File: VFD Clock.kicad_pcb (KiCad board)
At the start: 2 copper layers, 28 parts, among them U1 74HC595, U10 74HC595, U11 UDN2981A, U12 IV-11 VFD Tube, U13 74HC595, U14 UDN2981A, U15 IV-11 VFD Tube, U16 74HC595, U17 UDN2981A, U18 IV-11 VFD Tube, U19 XL6009 Module, U2 UDN2981A, U20 LM2596 Module, U3 IV-11 VFD Tube, U4 74HC595, U5 UDN2981A, U6 IV-11 VFD Tube, U7 74HC595, U8 UDN2981A, U9 IV-11 VFD Tube

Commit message: pcb layout updates. Locked in the tube positions
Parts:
- U12: value IV-11 VFD Tube -> Minute Right
- U15: value IV-11 VFD Tube -> Second Left
- U18: value IV-11 VFD Tube -> Second Right
- U3: value IV-11 VFD Tube -> Hour Left
- U6: value IV-11 VFD Tube -> Hour Right
- U9: value IV-11 VFD Tube -> Minute Left
- moved U20 121.2 mm to (138.1, 153.7), turned to 180 degrees
- moved U17 74.4 mm to (243.8, 81.8)
- moved U16 72.0 mm to (261.2, 119.0)
- moved U18 71.8 mm to (251.0, 100.0)
- moved U19 70.5 mm to (189.4, 152.4), turned to 180 degrees
- moved A1 52.9 mm to (214.5, 151.0), turned to 90 degrees
- moved U1 40.8 mm to (108.1, 116.4)
- moved U7 40.8 mm to (172.1, 119.4)
- moved U9 40.5 mm to (162.0, 100.0)
- moved U3 40.1 mm to (100.0, 100.0)
- moved U2 40.0 mm to (89.8, 82.6)
- moved U12 38.6 mm to (189.0, 100.0)
- moved U4 38.3 mm to (135.9, 117.2)
- moved U10 38.2 mm to (197.8, 119.4)
- moved U8 37.5 mm to (150.8, 83.0)
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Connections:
- net /D2 renamed /Mode_Button
- net /D3 renamed /Up_Button
- net /D4 renamed /Down_Button
- net /D5 renamed /Select_Button

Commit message: PCB layout changes
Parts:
- moved C10 317.5 mm to (88.0, 120.0), turned to 90 degrees
- moved C9 288.6 mm to (118.0, 120.0), turned to 90 degrees
- moved C8 259.9 mm to (148.0, 120.0), turned to 90 degrees
- moved C7 231.6 mm to (178.0, 120.0), turned to 90 degrees
- moved C1 199.6 mm to (221.0, 130.0), turned to 180 degrees
- moved C11 199.4 mm to (208.0, 120.0), turned to 90 degrees
- moved C12 168.7 mm to (239.0, 120.0), turned to 90 degrees
- moved U13 6.75 mm to (229.0, 115.0)
- moved U7 5.35 mm to (169.0, 115.0)
- moved U10 4.55 mm to (199.0, 115.0)
- moved U16 4.19 mm to (260.0, 115.0)
- moved U4 3.76 mm to (139.1, 115.2)
- moved U5 3.12 mm to (121.1, 84.0)
- moved U11 2.95 mm to (181.5, 84.0)
- moved U17 2.86 mm to (242.0, 84.0)
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
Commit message: pcb layout
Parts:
- moved U20 54.4 mm to (91.1, 126.3), turned to 0 degrees
- moved U19 42.8 mm to (154.6, 127.6), turned to 0 degrees
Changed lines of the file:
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@@
 		)
 		(property "Value" "UDN2981A"
-			(at -11 -3.74 0)
+			(at -10 -4.16 0)
 			(layer "F.Fab")
 			(effects
@@
 		)
 		(property "Value" "UDN2981A"
-			(at 10.46468 4.04836 90)
+			(at -10 -5 180)
 			(layer "F.Fab")
 			(effects
@@
 	(footprint "Custom Parts:LM2596 Module"
 		(layer "F.Cu")
-		(at 138.14 153.66 180)
+		(at 91.14 126.34)
 		(property "Reference" "U20"
-			(at 25.4 8.66 180)
+			(at 25.4 8.66 0)
 			(unlocked yes)
 			(layer "F.SilkS")
@@
 		)
 		(property "Value" "LM2596 Module"
-			(at 25.4 10.16 180)
+			(at 25.4 10.16 0)
 			(unlocked yes)
 			(layer "F.Fab")
@@
 		)
 		(property "Datasheet" ""
-			(at 0 0 180)
+			(at 0 0 0)
 			(unlocked yes)
 			(layer "F.Fab")
@@
 		)
 		(property "Description" "LM2596 Module from Aliexpress"
-			(at 0 0 180)
+			(at 0 0 0)
 			(unlocked yes)
 			(layer "F.Fab")
@@
 		(duplicate_pad_numbers_are_jumpers no)
 		(fp_line
-			(start 48 23)
+			(start 0 0)
 			(end 0 23)
 			(stroke
@@
 		)
 		(fp_line
-			(start 48 0)
-			(end 48 23)
+			(start 0 0)
+			(end 48 0)
 			(stroke
 				(width 0.1)
@@
 		)
 		(fp_line
-			(start 0 0)
-			(end 48 0)
+			(start 48 0)
+			(end 48 23)
 			(stroke
 				(width 0.1)
@@
 		)
 		(fp_line
-			(start 0 0)
+			(start 48 23)
 			(end 0 23)
 			(stroke
@@
 		)
 		(fp_text user "${REFERENCE}"
-			(at 25.4 11.66 180)
+			(at 25.4 11.66 0)
 			(unlocked yes)
 			(layer "F.Fab")
@@
 		)
 		(pad "1" thru_hole circle
-			(at 1.14 1.34 180)
+			(at 1.14 1.34)
 			(size 1.8 1.8)
 			(drill 1)
@@
 		)
 		(pad "2" thru_hole circle
-			(at 1.14 21.66 180)
+			(at 1.14 21.66)
 			(size 1.8 1.8)
 			(drill 1)
@@
 		)
 		(pad "3" thru_hole circle
-			(at 46.86 1.34 180)
+			(at 46.86 1.34)
 			(size 1.8 1.8)
 			(drill 1)
@@
 		)
 		(pad "4" thru_hole circle
-			(at 46.86 21.66 180)
+			(at 46.86 21.66)
 			(size 1.8 1.8)
 			(drill 1)
@@
 		)
 		(property "Value" "UDN2981A"
-			(at 10.46468 4.04836 90)
+			(at -10 -4.696 180)
 			(layer "F.Fab")
 			(effects
@@
 		)
 		(property "Value" "UDN2981A"
-			(at 10.46468 4.04836 90)
+			(at -10 -3.928 180)
 			(layer "F.Fab")
 			(effects
@@
 		)
 		(property "Value" "UDN2981A"
-			(at 10.46468 4.04836 90)
+			(at -10 -5.464 180)
 			(layer "F.Fab")
 			(effects
@@
 	(footprint "Custom Parts:XL6009 Module"
 		(layer "F.Cu")
-		(at 189.4394 152.4285 180)
+		(at 154.5606 127.5715)
 		(property "Reference" "U19"
-			(at 21 11 180)
+			(at 21 11 0)
 			(unlocked yes)
 			(layer "F.SilkS")
@@
 		)
 		(property "Value" "XL6009 Module"
-			(at 21 7.5 180)
+			(at 21 7.5 0)
 			(unlocked yes)
 			(layer "F.Fab")
@@
 		)
 		(property "Datasheet" ""
-			(at 0 0 180)
+			(at 0 0 0)
 			(unlocked yes)
 			(layer "F.Fab")
@@
 		)
 		(property "Description" "XL6009 Module from Aliexpress"
-			(at 0 0 180)
+			(at 0 0 0)
 			(unlocked yes)
 			(layer "F.Fab")
@@
 		(duplicate_pad_numbers_are_jumpers no)
 		(fp_line
-			(start 43 21)
-			(end 0 21)
+			(start 0 0)
+			(end 43 0)
 			(stroke
 				(width 0.1)
@@
 		)
 		(fp_line
-			(start 43 0)
-			(end 43 21)
+			(start 0 21)
+			(end 0 0)
 			(stroke
 				(width 0.1)
@@
 		)
 		(fp_line
-			(start 0 21)
-			(end 0 0)
+			(start 43 0)
+			(end 43 21)
 			(stroke
 				(width 0.1)
@@
 		)
 		(fp_line
-			(start 0 0)
-			(end 43 0)
+			(start 43 21)
+			(end 0 21)
 			(stroke
 				(width 0.1)
@@
 		)
 		(fp_line
-			(start 43.1038 21.082)
-			(end -0.0762 21.082)
+			(start -0.0762 21.082)
+			(end -0.0762 -0.1016)
 			(stroke
 				(width 0.05)
@@
 		)
 		(fp_line
-			(start 43.1038 -0.1016)
-			(end 43.1038 21.082)
+			(start -0.0508 -0.1016)
+			(end -0.0762 -0.1016)
 			(stroke
 				(width 0.05)
@@
 		)
 		(fp_line
-			(start -0.0508 -0.1016)
-			(end -0.0762 -0.1016)
+			(start 43.1038 -0.1016)
+			(end 43.1038 21.082)
 			(stroke
 				(width 0.05)
@@
 		)
 		(fp_line
-			(start -0.0762 21.082)
-			(end -0.0762 -0.1016)
+			(start 43.1038 21.082)
+			(end -0.0762 21.082)
 			(stroke
 				(width 0.05)
@@
 			(layer "F.CrtYd")
 		)
-		(fp_text user "Out-"
-			(at 36.9316 19.9898 180)
+		(fp_text user "In-"
+			(at 2.4638 19.8882 0)
 			(unlocked yes)
 			(layer "F.SilkS")
@@
 			)
 		)
-		(fp_text user "Out+"
-			(at 36.8808 2.1844 180)
+		(fp_text user "In+"
+			(at 2.6162 2.2352 0)
 			(unlocked yes)
 			(layer "F.SilkS")
@@
 			)
 		)
-		(fp_text user "In+"
-			(at 2.6162 2.2352 180)
+		(fp_text user "Out+"
+			(at 36.8808 2.1844 0)
 			(unlocked yes)
 			(layer "F.SilkS")
@@
 			)
 		)
-		(fp_text user "In-"
-			(at 2.4638 19.8882 180)
+		(fp_text user "Out-"
+			(at 36.9316 19.9898 0)
 			(unlocked yes)
 			(layer "F.SilkS")
@@
 		)
 		(fp_text user "${REFERENCE}"
-			(at 21 9 180)
+			(at 21 9 0)
 			(unlocked yes)
 			(layer "F.Fab")
@@
 		)
 		(pad "1" thru_hole circle
-			(at 1.18 1.61 180)
+			(at 1.18 1.61)
 			(size 1.8 1.8)
 			(drill 1)
@@
 		)
 		(pad "2" thru_hole circle
-			(at 1.18 19.39 180)
+			(at 1.18 19.39)
 			(size 1.8 1.8)
 			(drill 1)
@@
 		)
 		(pad "3" thru_hole circle
-			(at 41.82 1.61 180)
+			(at 41.82 1.61)
 			(size 1.8 1.8)
 			(drill 1)
@@
 		)
 		(pad "4" thru_hole circle
-			(at 41.82 19.39 180)
+			(at 41.82 19.39)
 			(size 1.8 1.8)
 			(drill 1)
@@
 		)
 		(property "Value" "UDN2981A"
-			(at 10.46468 4.04836 90)
+			(at -10 -5.232 180)
 			(layer "F.Fab")
 			(effects

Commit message: minor changes
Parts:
- added J2: Mode Button, Connector_JST:JST_XH_B2B-XH-A_1x02_P2.50mm_Vertical, F.Cu at (187.5, 143.5)
- added J3: Up Button, Connector_JST:JST_XH_B2B-XH-A_1x02_P2.50mm_Vertical, F.Cu at (197.5, 143.5)
- added J4: Down Button, Connector_JST:JST_XH_B2B-XH-A_1x02_P2.50mm_Vertical, F.Cu at (207.0, 143.5)
- added J5: Select Button, Connector_JST:JST_XH_B2B-XH-A_1x02_P2.50mm_Vertical, F.Cu at (217.0, 143.5)
- moved A1 152.9 mm to (68.0, 107.0), turned to 0 degrees
- moved C1 142.0 mm to (82.5, 98.5)
- moved U19 17.5 mm to (137.1, 126.6)
- moved U20 4.68 mm to (86.5, 125.5)
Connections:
- A1 pad 10: /Power LED -> unconnected-(A1-D7-Pad10)

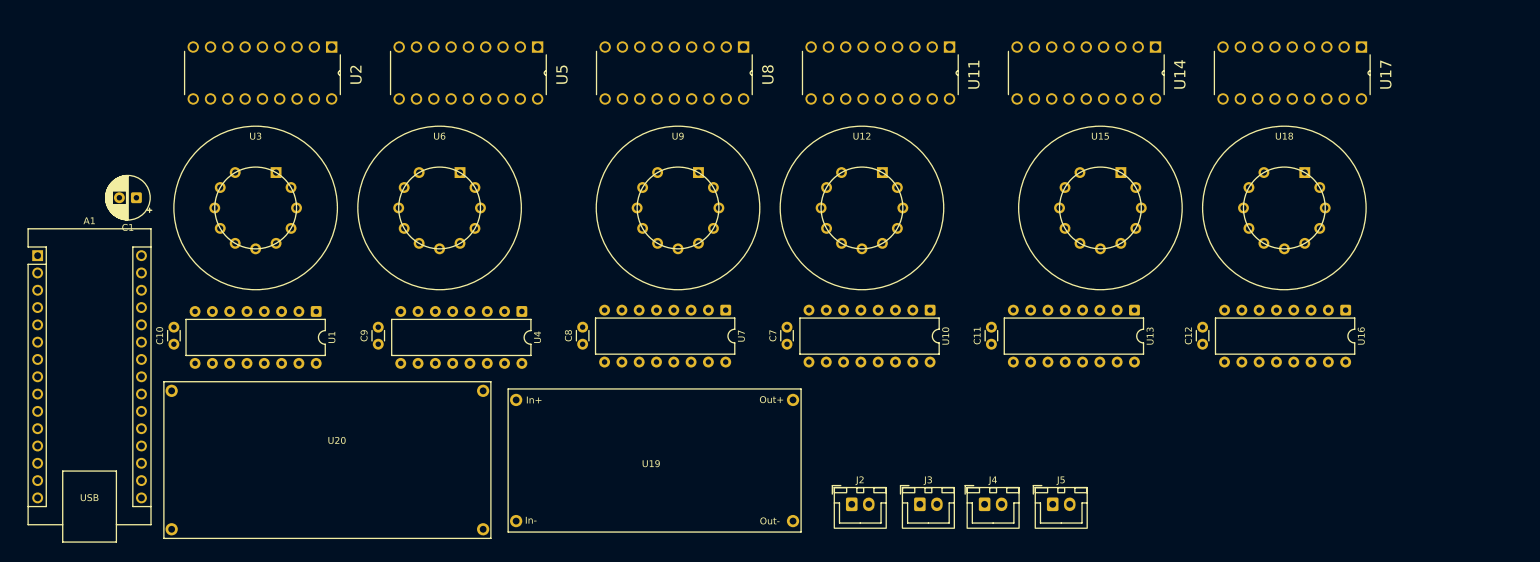
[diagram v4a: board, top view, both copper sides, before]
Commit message: Created custom ds3231 module and added it to schematic and pcb
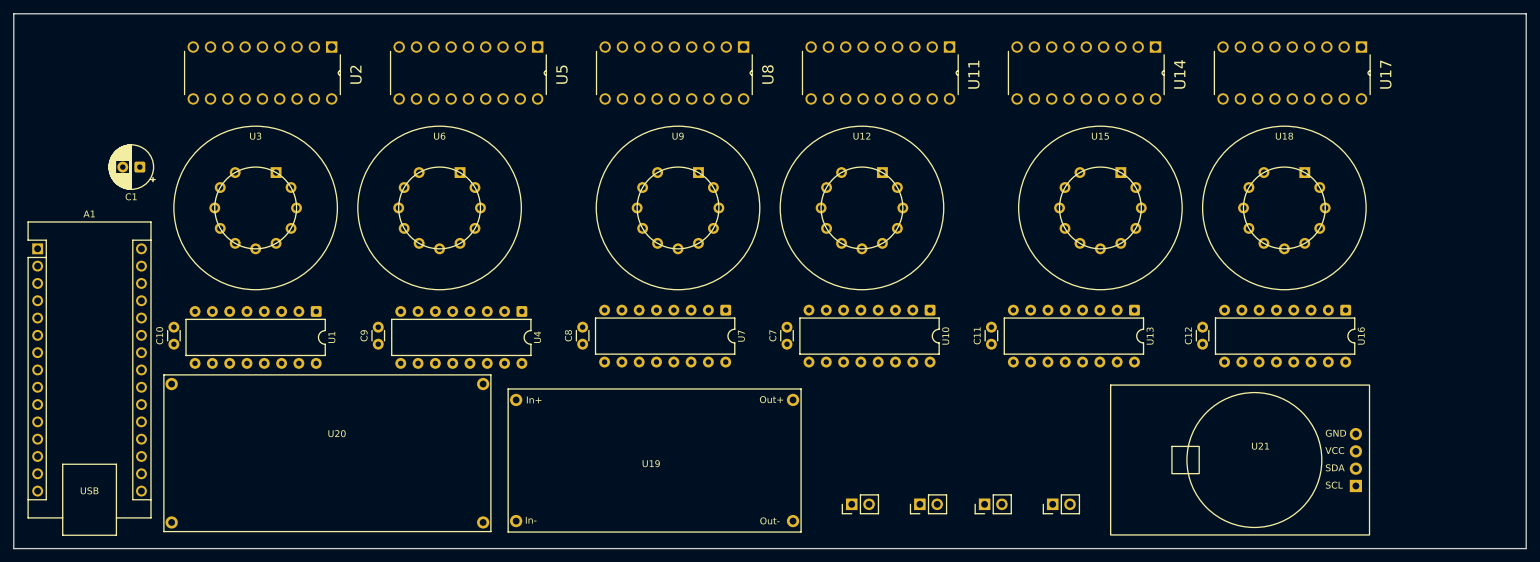
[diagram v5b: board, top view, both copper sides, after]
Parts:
- added U21: DS3231 Module, Custom Parts:DS3231 Module, F.Cu at (225.5, 126.0)
- J2, J3, J4, J5: footprint Connector_JST:JST_XH_B2B-XH-A_1x02_P2.50mm_Vertical -> Connector_PinHeader_2.54mm:PinHeader_1x02_P2.54mm_Vertical
- moved C1 4.53 mm to (83.0, 94.0)
- moved A1 1.00 mm to (68.0, 106.0)
- moved U20 1.00 mm to (86.5, 124.5)
- turned J2 to 90 degrees
- turned J3 to 90 degrees
- turned J4 to 90 degrees
- turned J5 to 90 degrees
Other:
- board outline added: 222 x 78.5 mm

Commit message: close to finishing pcb
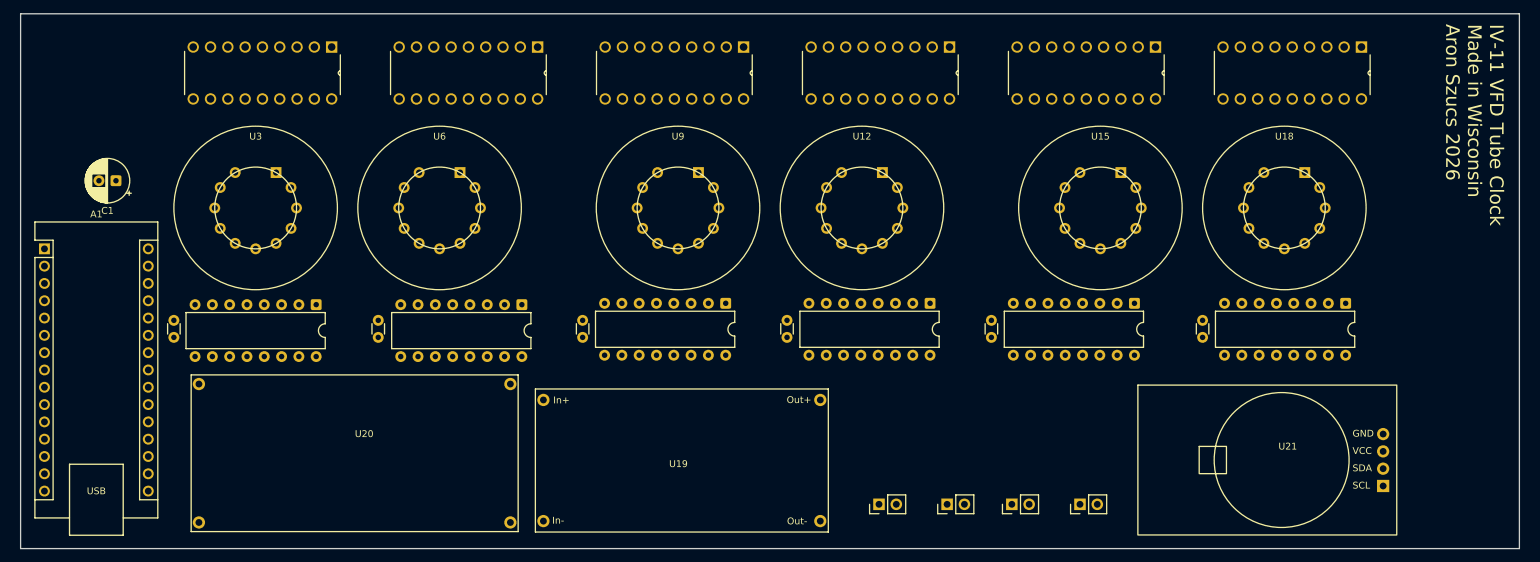
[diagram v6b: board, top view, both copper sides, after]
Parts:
- moved C1 4.03 mm to (79.5, 96.0)
- moved J2 4.00 mm to (191.5, 143.5)
- moved J3 4.00 mm to (201.5, 143.5)
- moved J4 4.00 mm to (211.0, 143.5)
- moved J5 4.00 mm to (221.0, 143.5)
- moved U19 4.00 mm to (141.1, 126.6)
- moved U20 4.00 mm to (90.5, 124.5)
- moved U21 4.00 mm to (229.5, 126.0)
- moved C10 1.00 mm to (88.0, 119.0)
- moved C11 1.00 mm to (208.0, 119.0)
- moved C12 1.00 mm to (239.0, 119.0)
- moved C7 1.00 mm to (178.0, 119.0)
- moved C8 1.00 mm to (148.0, 119.0)
- moved C9 1.00 mm to (118.0, 119.0)
- moved U10 1.00 mm to (199.0, 114.0)
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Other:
- board size 222 x 78.5 mm -> 220 x 78.5 mm
- board text added: "IV-11 VFD Tube Clock Made in Wisconsin Aron Szucs 2026"

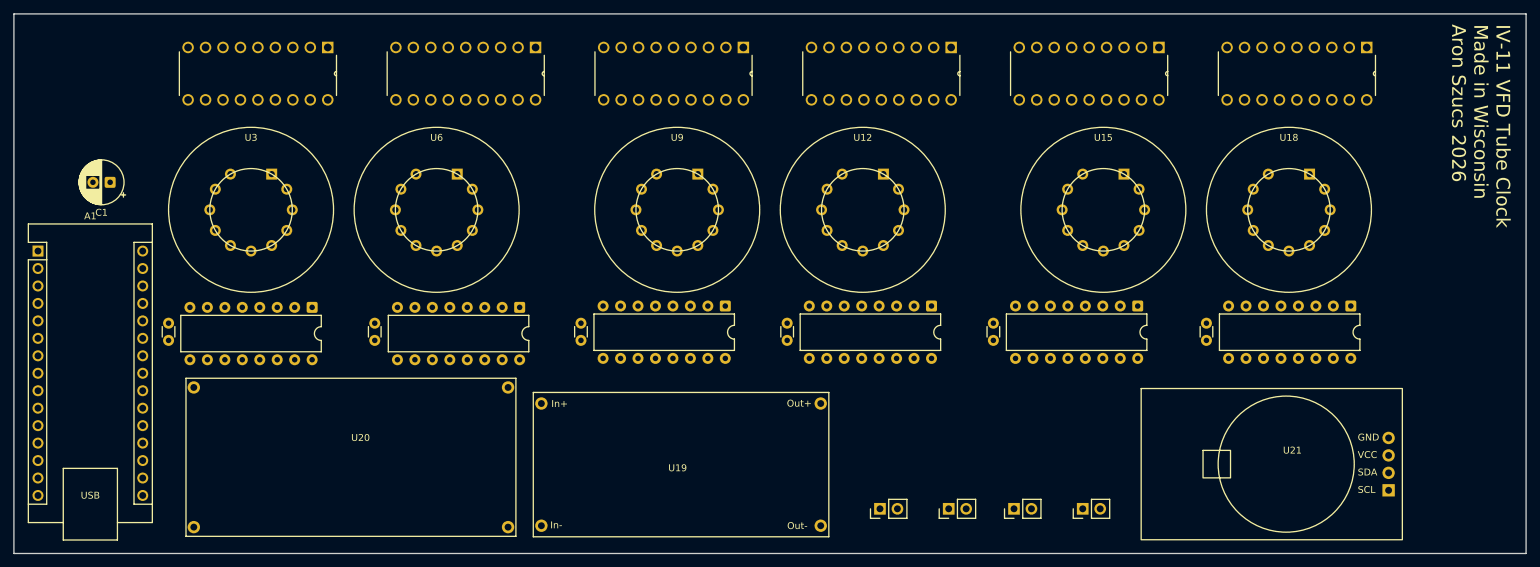
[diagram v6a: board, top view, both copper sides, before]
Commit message: mounting holes
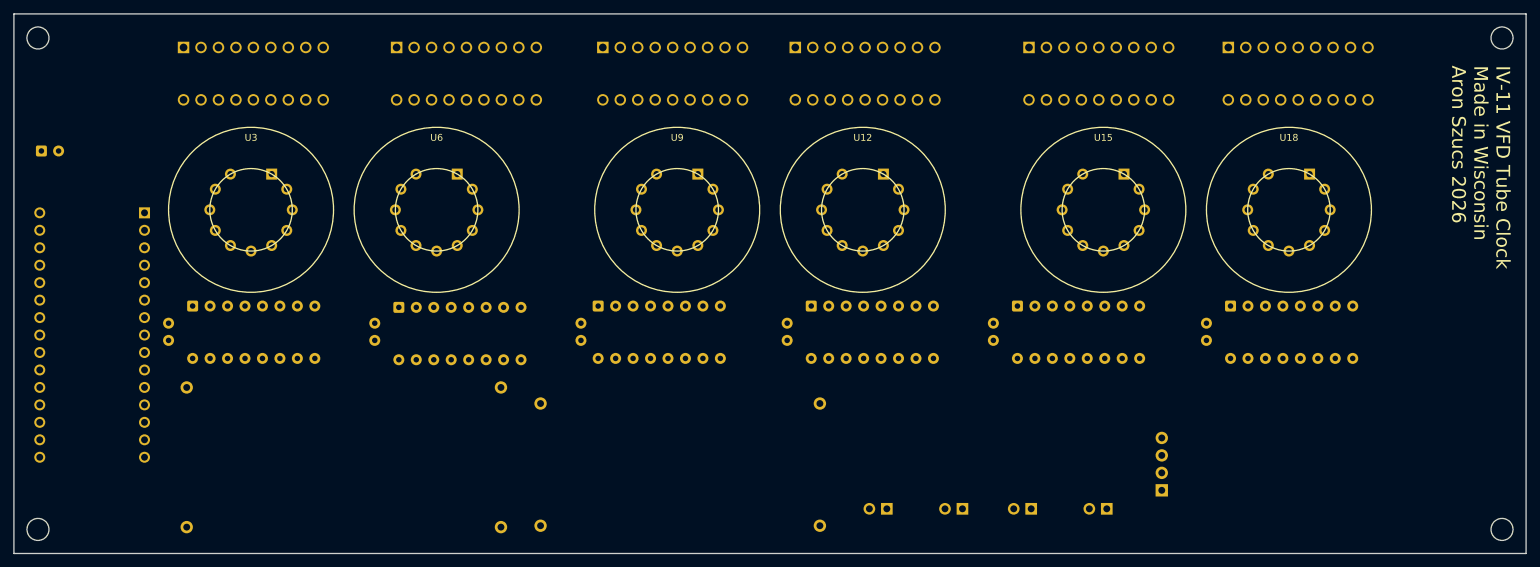
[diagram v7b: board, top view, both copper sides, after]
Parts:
- added REF**: MountingHole_3.2mm_M3, MountingHole:MountingHole_3.2mm_M3, F.Cu at (69.0, 75.0)
- added REF**: MountingHole_3.2mm_M3, MountingHole:MountingHole_3.2mm_M3, F.Cu at (282.0, 146.5)
- added REF**: MountingHole_3.2mm_M3, MountingHole:MountingHole_3.2mm_M3, F.Cu at (69.0, 146.5)
- added REF**: MountingHole_3.2mm_M3, MountingHole:MountingHole_3.2mm_M3, F.Cu at (282.0, 75.0)
- A1, C1, C10, C11, C12, C7, C8, C9, J2, J3, J4, J5, U1, U10, U11, U13, U14, U16, U17, U19, U2, U20, U21, U4, U5, U7, U8: moved to B.Cu
- moved U20 47.0 mm to (137.5, 124.5), turned to 180 degrees
- moved U19 42.9 mm to (183.9, 126.6), turned to 180 degrees
- moved U21 39.0 mm to (268.5, 126.0), turned to 180 degrees
- moved U14 21.7 mm to (233.5, 84.0)
- moved U17 20.5 mm to (262.5, 84.0)
- moved U5 20.4 mm to (141.5, 84.0)
- moved U8 20.2 mm to (171.5, 84.0)
- moved U2 19.7 mm to (110.5, 84.0)
- moved U7 18.5 mm to (150.5, 114.0)
- moved U11 18.0 mm to (199.5, 84.0)
- moved U4 17.6 mm to (121.5, 114.2)
- moved U10 17.5 mm to (181.5, 114.0)
- moved U13 17.5 mm to (211.5, 114.0)
- moved U16 17.5 mm to (242.5, 114.0)
- moved U1 17.4 mm to (91.5, 114.0)
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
